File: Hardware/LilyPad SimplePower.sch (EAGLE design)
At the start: 16 parts, among them U1 MCP73831

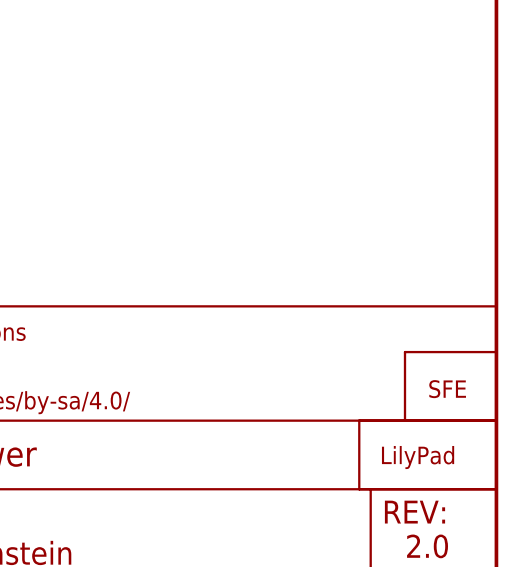
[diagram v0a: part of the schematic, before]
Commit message: Updating round two protos again to fix missing drill hits.
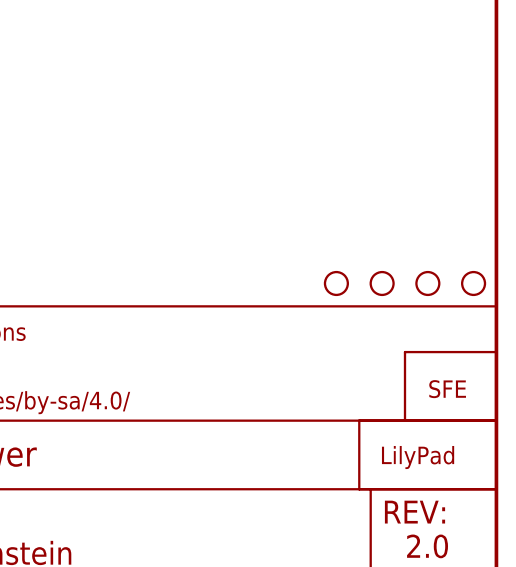
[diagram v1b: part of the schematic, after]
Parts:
- added STANDOFF1, STANDOFF2, STANDOFF3, STANDOFF4: SEW-HOLE-NO-PAD, Local Library:SEW-HOLE-NO-PAD
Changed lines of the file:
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@@
 <layer number="54" name="bGND_GNDA" color="1" fill="9" visible="no" active="no"/>
 <layer number="56" name="wert" color="7" fill="1" visible="no" active="no"/>
+<layer number="57" name="tCAD" color="7" fill="1" visible="no" active="no"/>
 <layer number="91" name="Nets" color="2" fill="1" visible="yes" active="yes"/>
 <layer number="92" name="Busses" color="1" fill="1" visible="yes" active="yes"/>
@@
 <layer number="97" name="Info" color="7" fill="1" visible="yes" active="yes"/>
 <layer number="98" name="Guide" color="6" fill="1" visible="yes" active="yes"/>
+<layer number="99" name="SpiceOrder" color="7" fill="1" visible="no" active="no"/>
 <layer number="100" name="Muster" color="7" fill="1" visible="no" active="no"/>
 <layer number="101" name="Patch_Top" color="12" fill="4" visible="yes" active="yes"/>
@@
 <layer number="108" name="tplace-old" color="10" fill="1" visible="yes" active="yes"/>
 <layer number="109" name="ref-old" color="11" fill="1" visible="yes" active="yes"/>
+<layer number="110" name="fp0" color="7" fill="1" visible="yes" active="yes"/>
+<layer number="111" name="LPC17xx" color="7" fill="1" visible="yes" active="yes"/>
+<layer number="112" name="tSilk" color="7" fill="1" visible="yes" active="yes"/>
+<layer number="113" name="IDFDebug" color="4" fill="1" visible="yes" active="yes"/>
 <layer number="116" name="Patch_BOT" color="9" fill="4" visible="yes" active="yes"/>
 <layer number="121" name="_tsilk" color="7" fill="1" visible="yes" active="yes"/>
 <layer number="122" name="_bsilk" color="7" fill="1" visible="yes" active="yes"/>
+<layer number="123" name="tTestmark" color="7" fill="1" visible="yes" active="yes"/>
+<layer number="124" name="bTestmark" color="7" fill="1" visible="yes" active="yes"/>
 <layer number="125" name="_tNames" color="7" fill="1" visible="no" active="yes"/>
+<layer number="126" name="_bNames" color="7" fill="1" visible="yes" active="yes"/>
+<layer number="127" name="_tValues" color="7" fill="1" visible="yes" active="yes"/>
+<layer number="128" name="_bValues" color="7" fill="1" visible="yes" active="yes"/>
+<layer number="131" name="tAdjust" color="7" fill="1" visible="yes" active="yes"/>
+<layer number="132" name="bAdjust" color="7" fill="1" visible="yes" active="yes"/>
 <layer number="144" name="Drill_legend" color="7" fill="1" visible="no" active="yes"/>
+<layer number="150" name="Notes" color="7" fill="1" visible="yes" active="yes"/>
 <layer number="151" name="HeatSink" color="7" fill="1" visible="yes" active="yes"/>
+<layer number="152" name="_bDocu" color="7" fill="1" visible="yes" active="yes"/>
+<layer number="153" name="FabDoc1" color="7" fill="1" visible="yes" active="yes"/>
+<layer number="154" name="FabDoc2" color="7" fill="1" visible="yes" active="yes"/>
+<layer number="155" name="FabDoc3" color="7" fill="1" visible="yes" active="yes"/>
 <layer number="199" name="Contour" color="7" fill="1" visible="yes" active="yes"/>
 <layer number="200" name="200bmp" color="7" fill="1" visible="yes" active="yes"/>
@@
 <layer number="223" name="223bmp" color="24" fill="1" visible="no" active="no"/>
 <layer number="224" name="224bmp" color="25" fill="1" visible="no" active="no"/>
+<layer number="248" name="Housing" color="7" fill="1" visible="yes" active="yes"/>
+<layer number="249" name="Edge" color="7" fill="1" visible="yes" active="yes"/>
 <layer number="250" name="Descript" color="3" fill="1" visible="no" active="no"/>
 <layer number="251" name="SMDround" color="12" fill="11" visible="no" active="no"/>
@@
 <part name="U$6" library="SparkFun-Aesthetics" deviceset="REVISION" device=""/>
 <part name="U$1" library="LilyPad-Wearables" deviceset="LOGO-LP" device="LP"/>
+<part name="STANDOFF1" library="Local Library" deviceset="SEW-HOLE-NO-PAD" device=""/>
+<part name="STANDOFF2" library="Local Library" deviceset="SEW-HOLE-NO-PAD" device=""/>
+<part name="STANDOFF3" library="Local Library" deviceset="SEW-HOLE-NO-PAD" device=""/>
+<part name="STANDOFF4" library="Local Library" deviceset="SEW-HOLE-NO-PAD" device=""/>
 </parts>
 <sheets>
@@
 <instance part="U$6" gate="G$1" x="148.082" y="6.858"/>
 <instance part="U$1" gate="G$1" x="236.22" y="17.78"/>
+<instance part="STANDOFF1" gate="G$1" x="246.38" y="38.1"/>
+<instance part="STANDOFF2" gate="G$1" x="241.3" y="38.1"/>
+<instance part="STANDOFF3" gate="G$1" x="236.22" y="38.1"/>
+<instance part="STANDOFF4" gate="G$1" x="231.14" y="38.1"/>
 </instances>
 <busses>

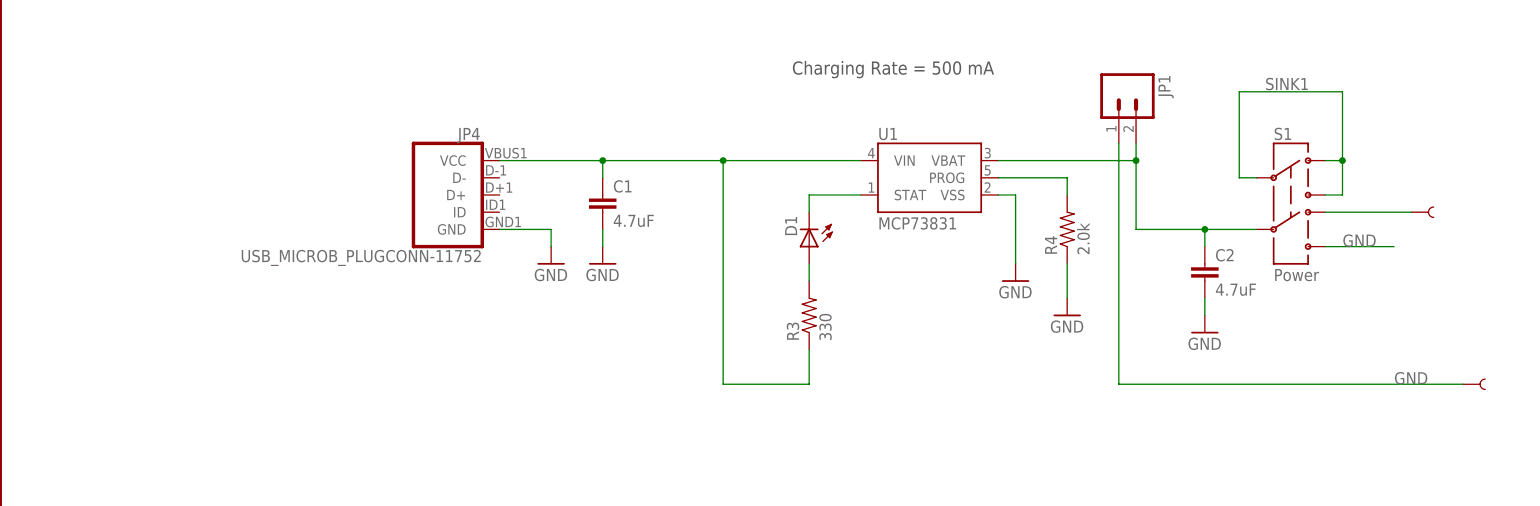
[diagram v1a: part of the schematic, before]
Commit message: Cleaning up schematic layout
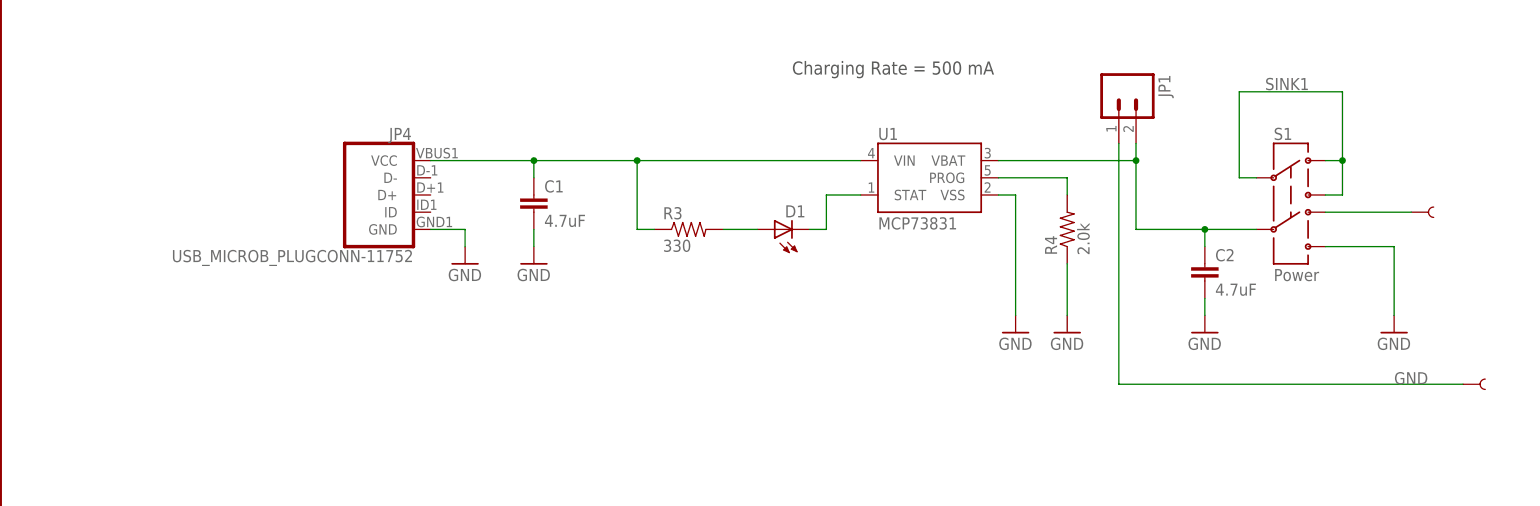
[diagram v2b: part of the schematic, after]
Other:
- moved on the sheet: C1, D1, JP4, R3
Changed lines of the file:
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@@
 <?xml version="1.0" encoding="utf-8"?>
 <!DOCTYPE eagle SYSTEM "eagle.dtd">
-<eagle version="6.6.0">
+<eagle version="7.1.0">
 <drawing>
 <settings>
@@
 <part name="STANDOFF3" library="Local Library" deviceset="SEW-HOLE-NO-PAD" device=""/>
 <part name="STANDOFF4" library="Local Library" deviceset="SEW-HOLE-NO-PAD" device=""/>
+<part name="GND6" library="SparkFun-Aesthetics" deviceset="GND" device=""/>
 </parts>
 <sheets>
@@
 <instance part="JP3" gate="G$1" x="241.3" y="25.4"/>
 <instance part="U1" gate="G$1" x="137.16" y="116.84"/>
-<instance part="JP4" gate="G$1" x="66.04" y="114.3" rot="MR0"/>
-<instance part="GND1" gate="1" x="81.28" y="104.14"/>
-<instance part="C1" gate="G$1" x="88.9" y="111.76"/>
-<instance part="GND2" gate="1" x="88.9" y="104.14"/>
-<instance part="R3" gate="G$1" x="119.38" y="96.52" rot="R90"/>
-<instance part="D1" gate="G$1" x="119.38" y="106.68" rot="R180"/>
+<instance part="JP4" gate="G$1" x="55.88" y="114.3" rot="MR0"/>
+<instance part="GND1" gate="1" x="68.58" y="104.14"/>
+<instance part="C1" gate="G$1" x="78.74" y="111.76"/>
+<instance part="GND2" gate="1" x="78.74" y="104.14"/>
+<instance part="R3" gate="G$1" x="101.6" y="109.22"/>
+<instance part="D1" gate="G$1" x="114.3" y="109.22" rot="R90"/>
 <instance part="C2" gate="G$1" x="177.8" y="101.6"/>
-<instance part="GND3" gate="1" x="149.86" y="101.6"/>
+<instance part="GND3" gate="1" x="149.86" y="93.98"/>
 <instance part="GND4" gate="1" x="177.8" y="93.98"/>
 <instance part="R4" gate="G$1" x="157.48" y="109.22" rot="R90"/>
-<instance part="GND5" gate="1" x="157.48" y="96.52"/>
+<instance part="GND5" gate="1" x="157.48" y="93.98"/>
 <instance part="U$6" gate="G$1" x="148.082" y="6.858"/>
 <instance part="U$1" gate="G$1" x="236.22" y="17.78"/>
@@
 <instance part="STANDOFF3" gate="G$1" x="236.22" y="38.1"/>
 <instance part="STANDOFF4" gate="G$1" x="231.14" y="38.1"/>
+<instance part="GND6" gate="1" x="205.74" y="93.98"/>
 </instances>
 <busses>
@@
 <segment>
 <pinref part="JP4" gate="G$1" pin="GND"/>
-<wire x1="73.66" y1="109.22" x2="81.28" y2="109.22" width="0.1524" layer="91"/>
+<wire x1="63.5" y1="109.22" x2="68.58" y2="109.22" width="0.1524" layer="91"/>
 <pinref part="GND1" gate="1" pin="GND"/>
-<wire x1="81.28" y1="109.22" x2="81.28" y2="106.68" width="0.1524" layer="91"/>
+<wire x1="68.58" y1="109.22" x2="68.58" y2="106.68" width="0.1524" layer="91"/>
 </segment>
 <segment>
 <pinref part="C1" gate="G$1" pin="2"/>
 <pinref part="GND2" gate="1" pin="GND"/>
-<wire x1="88.9" y1="109.22" x2="88.9" y2="106.68" width="0.1524" layer="91"/>
+<wire x1="78.74" y1="109.22" x2="78.74" y2="106.68" width="0.1524" layer="91"/>
 </segment>
 <segment>
@@
 <pinref part="GND3" gate="1" pin="GND"/>
 <wire x1="147.32" y1="114.3" x2="149.86" y2="114.3" width="0.1524" layer="91"/>
-<wire x1="149.86" y1="114.3" x2="149.86" y2="104.14" width="0.1524" layer="91"/>
+<wire x1="149.86" y1="114.3" x2="149.86" y2="96.52" width="0.1524" layer="91"/>
 </segment>
 <segment>
@@
 <pinref part="R4" gate="G$1" pin="1"/>
 <pinref part="GND5" gate="1" pin="GND"/>
-<wire x1="157.48" y1="104.14" x2="157.48" y2="99.06" width="0.1524" layer="91"/>
+<wire x1="157.48" y1="104.14" x2="157.48" y2="96.52" width="0.1524" layer="91"/>
 </segment>
 <segment>
 <wire x1="195.58" y1="106.68" x2="205.74" y2="106.68" width="0.1524" layer="91"/>
-<label x="198.12" y="106.68" size="1.778" layer="95"/>
 <pinref part="S1" gate="G$1" pin="6"/>
+<pinref part="GND6" gate="1" pin="GND"/>
+<wire x1="205.74" y1="106.68" x2="205.74" y2="96.52" width="0.2032" layer="91"/>
 </segment>
 </net>
@@
 <segment>
 <pinref part="JP4" gate="G$1" pin="VCC"/>
-<wire x1="73.66" y1="119.38" x2="88.9" y2="119.38" width="0.1524" layer="91"/>
+<wire x1="63.5" y1="119.38" x2="78.74" y2="119.38" width="0.1524" layer="91"/>
 <pinref part="U1" gate="G$1" pin="VIN"/>
-<junction x="88.9" y="119.38"/>
-<wire x1="88.9" y1="119.38" x2="106.68" y2="119.38" width="0.1524" layer="91"/>
+<junction x="78.74" y="119.38"/>
+<wire x1="78.74" y1="119.38" x2="93.98" y2="119.38" width="0.1524" layer="91"/>
 <pinref part="C1" gate="G$1" pin="1"/>
-<wire x1="106.68" y1="119.38" x2="127" y2="119.38" width="0.1524" layer="91"/>
-<wire x1="88.9" y1="119.38" x2="88.9" y2="116.84" width="0.1524" layer="91"/>
+<wire x1="93.98" y1="119.38" x2="127" y2="119.38" width="0.1524" layer="91"/>
+<wire x1="78.74" y1="119.38" x2="78.74" y2="116.84" width="0.1524" layer="91"/>
 <pinref part="R3" gate="G$1" pin="1"/>
-<wire x1="119.38" y1="91.44" x2="119.38" y2="86.36" width="0.1524" layer="91"/>
-<wire x1="119.38" y1="86.36" x2="106.68" y2="86.36" width="0.1524" layer="91"/>
-<wire x1="106.68" y1="86.36" x2="106.68" y2="119.38" width="0.1524" layer="91"/>
-<junction x="106.68" y="119.38"/>
+<wire x1="96.52" y1="109.22" x2="93.98" y2="109.22" width="0.1524" layer="91"/>
+<wire x1="93.98" y1="109.22" x2="93.98" y2="119.38" width="0.1524" layer="91"/>
+<junction x="93.98" y="119.38"/>
 </segment>
 </net>
@@
 <segment>
 <pinref part="U1" gate="G$1" pin="STAT"/>
-<wire x1="127" y1="114.3" x2="119.38" y2="114.3" width="0.1524" layer="91"/>
+<wire x1="127" y1="114.3" x2="121.92" y2="114.3" width="0.1524" layer="91"/>
+<wire x1="121.92" y1="114.3" x2="121.92" y2="109.22" width="0.1524" layer="91"/>
 <pinref part="D1" gate="G$1" pin="C"/>
-<wire x1="119.38" y1="114.3" x2="119.38" y2="111.76" width="0.1524" layer="91"/>
+<wire x1="121.92" y1="109.22" x2="119.38" y2="109.22" width="0.1524" layer="91"/>
 </segment>
 </net>
@@
 <pinref part="D1" gate="G$1" pin="A"/>
 <pinref part="R3" gate="G$1" pin="2"/>
-<wire x1="119.38" y1="104.14" x2="119.38" y2="101.6" width="0.1524" layer="91"/>
-</segment>
-</net>
+<wire x1="111.76" y1="109.22" x2="106.68" y2="109.22" width="0.1524" layer="91"/>
+</segment>
+</net>

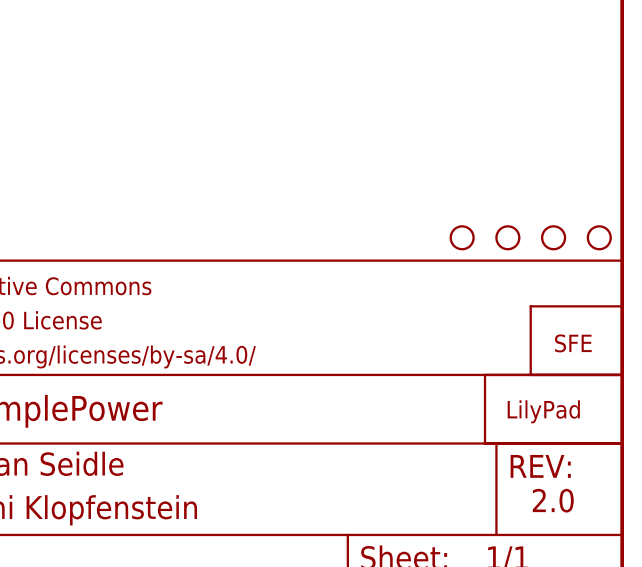
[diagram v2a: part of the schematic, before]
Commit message: added board fiducials
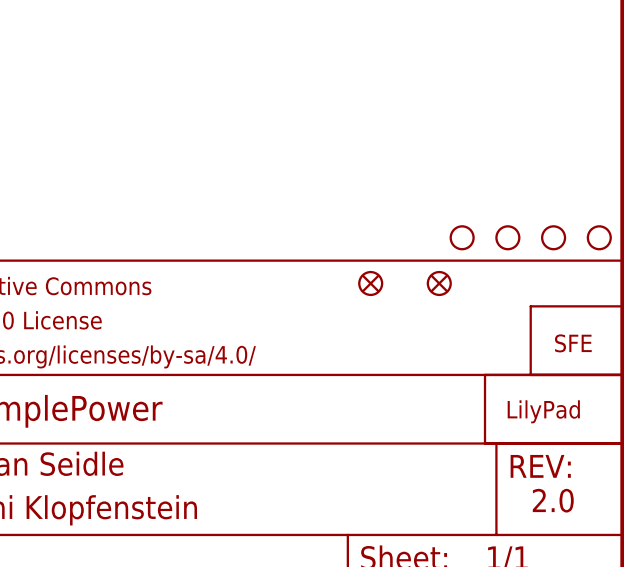
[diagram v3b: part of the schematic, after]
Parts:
- added FID1, FID2: FIDUCIAL1X2, SparkFun-Aesthetics:FIDUCIAL1X2
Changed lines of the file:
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@@
 <?xml version="1.0" encoding="utf-8"?>
 <!DOCTYPE eagle SYSTEM "eagle.dtd">
-<eagle version="7.1.0">
+<eagle version="6.6.0">
 <drawing>
 <settings>
@@
 <part name="STANDOFF4" library="Local Library" deviceset="SEW-HOLE-NO-PAD" device=""/>
 <part name="GND6" library="SparkFun-Aesthetics" deviceset="GND" device=""/>
+<part name="FID1" library="SparkFun-Aesthetics" deviceset="FIDUCIAL" device="1X2"/>
+<part name="FID2" library="SparkFun-Aesthetics" deviceset="FIDUCIAL" device="1X2"/>
 </parts>
 <sheets>
@@
 <instance part="STANDOFF4" gate="G$1" x="231.14" y="38.1"/>
 <instance part="GND6" gate="1" x="205.74" y="93.98"/>
+<instance part="FID1" gate="G$1" x="220.98" y="33.02"/>
+<instance part="FID2" gate="G$1" x="228.6" y="33.02"/>
 </instances>
 <busses>
